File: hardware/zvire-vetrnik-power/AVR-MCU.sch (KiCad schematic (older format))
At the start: 38 parts, among them J10 AC frequency sense, J11 AVR-ISP-6, J12 ACS712_2, J13 ACS712, Q13 BC847, Q14 BC846, SW1 AVR RESET, U1 LTV-847, U8 L78L05_TO92, U9 ATmega8-16PU, Y1 16MHz

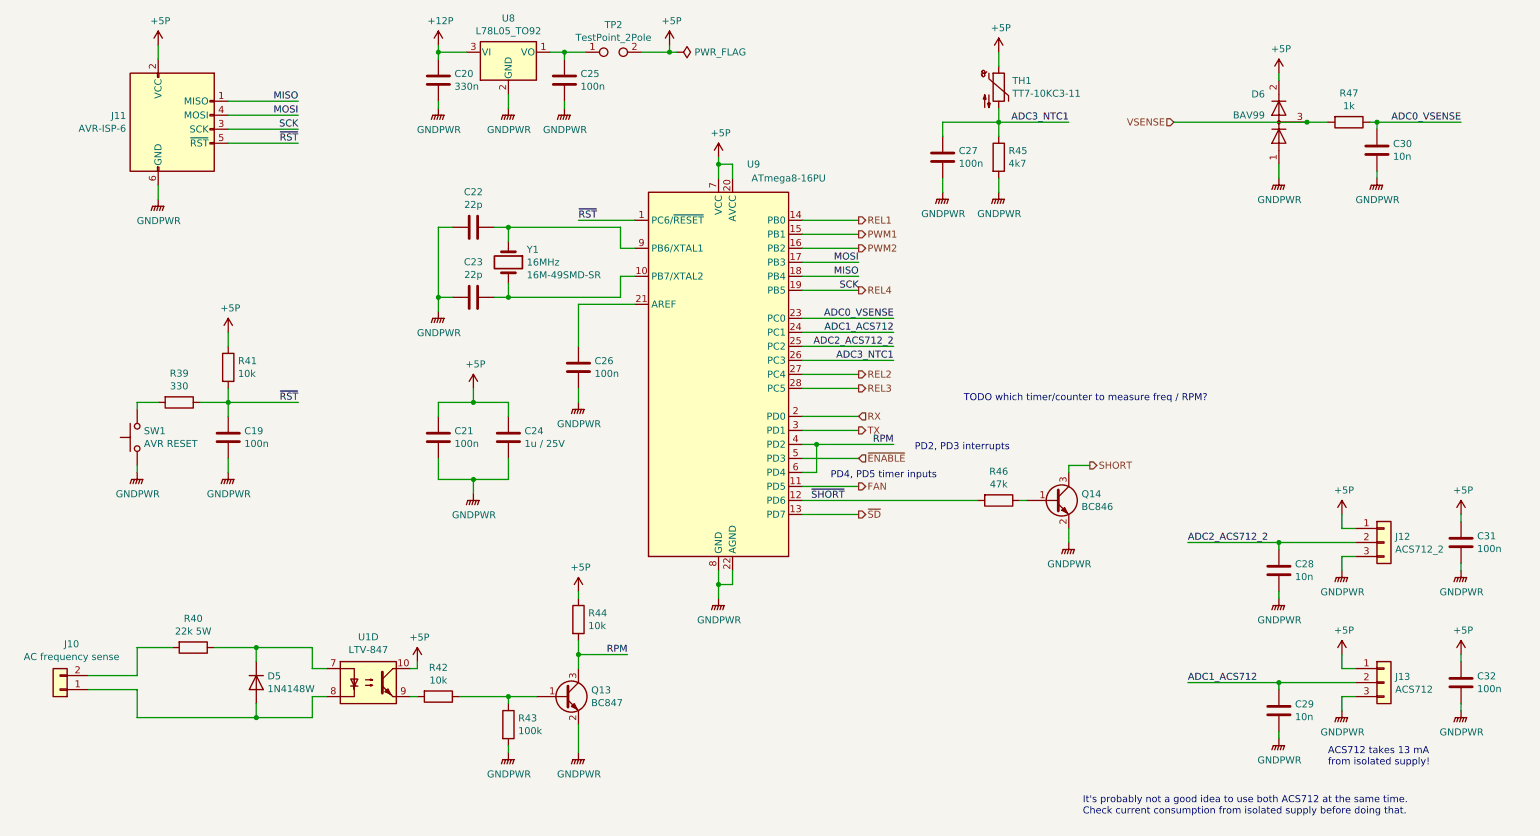
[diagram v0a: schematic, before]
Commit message: Vyrobena verze power PCB
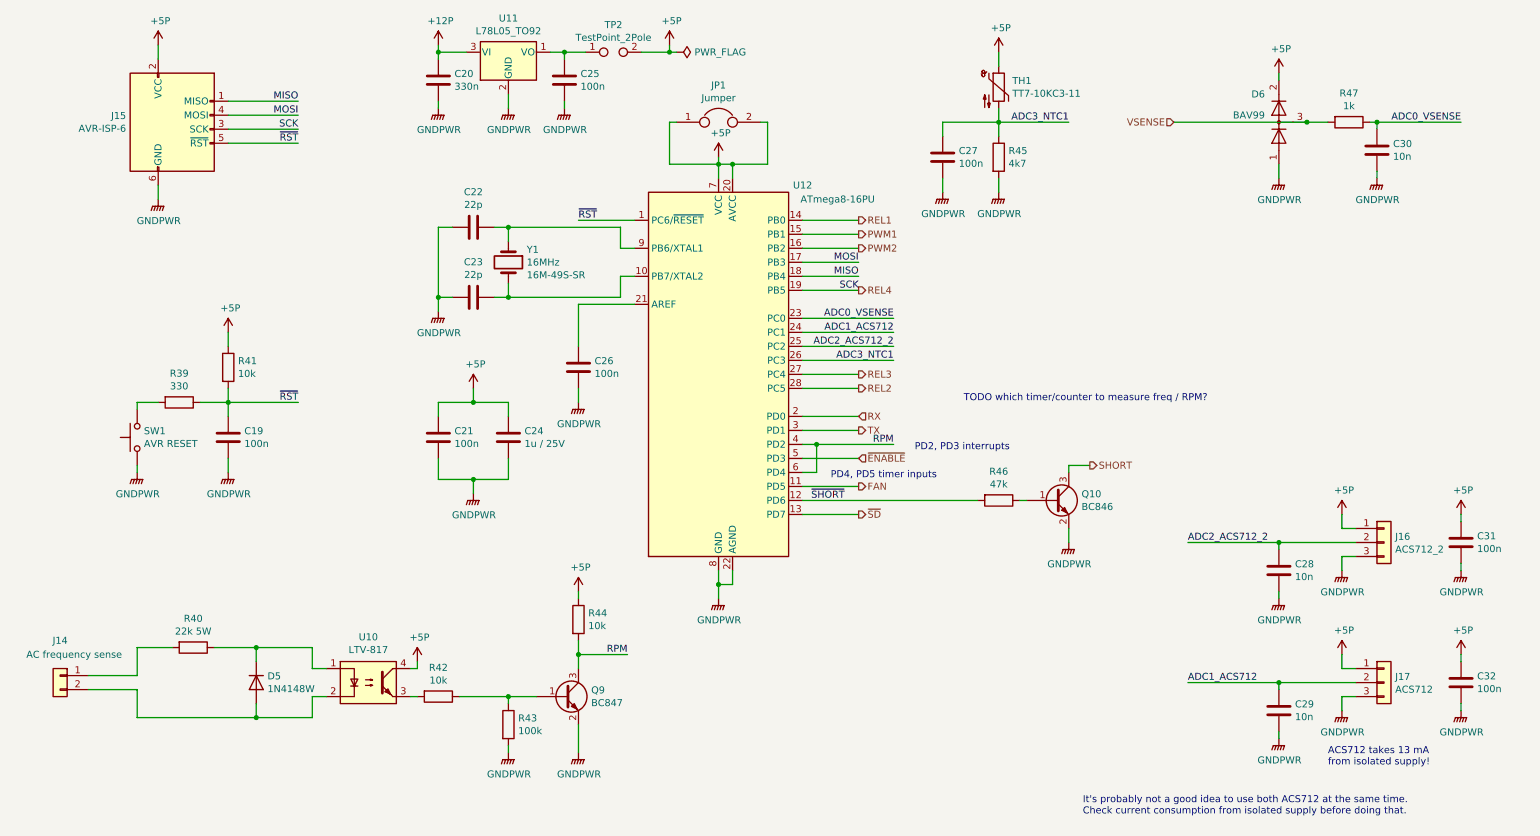
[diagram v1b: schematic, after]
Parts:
- removed U1: LTV-847, Package_DIP:DIP-16_W7.62mm, symbol Isolator:LTV-847
- added JP1: Jumper, Resistor_SMD:R_1206_3216Metric_Pad1.30x1.75mm_HandSolder, symbol Device:Jumper
- added U10: LTV-817, Package_DIP:DIP-4_W7.62mm, symbol Isolator:LTV-817
- TH1: footprint Resistor_THT:R_Axial_DIN0204_L3.6mm_D1.6mm_P2.54mm_Vertical -> Connector_Molex:Molex_KK-254_AE-6410-02A_1x02_P2.54mm_Vertical
- U11: renamed from U8; footprint Package_TO_SOT_THT:TO-92_Inline -> Package_TO_SOT_THT:TO-92L_HandSolder
- U12: renamed from U9; footprint Package_DIP:DIP-28_W7.62mm -> Package_DIP:DIP-28_W7.62mm_Socket
- Y1: footprint Crystal:Crystal_SMD_HC49-SD_HandSoldering -> Crystal:Crystal_HC49-U_Vertical; TME https://www.tme.eu/cz/details/16m-49smd-sr/krystalove-rezon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 -> https://www.tme.eu/cz/details/16m-49s-sr/krystalove-rezonat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; TME Symbol 16M-49SMD-SR -> 16M-49S-SR
- renumbered J10 to J14, J11 to J15, J12 to J16, J13 to J17, Q14 to Q10, Q13 to Q9
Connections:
- net +5P: now also JP1.1, JP1.2, U10.4
- net REL2: now also U12.28 (PC5); no longer U12.27 (PC4)
- net REL3: now also U12.27 (PC4); no longer U12.28 (PC5)
- net at R42.2: now also U10.3
- net at D5.1 (K), R40.1: now also U10.1
- net at D5.2 (A): now also J14.2 (Pin_2), U10.2; no longer J14.1 (Pin_1)
- net at R40.2: now also J14.1 (Pin_1); no longer J14.2 (Pin_2)

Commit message: Add filter cap for noise immunity in RPM circuit
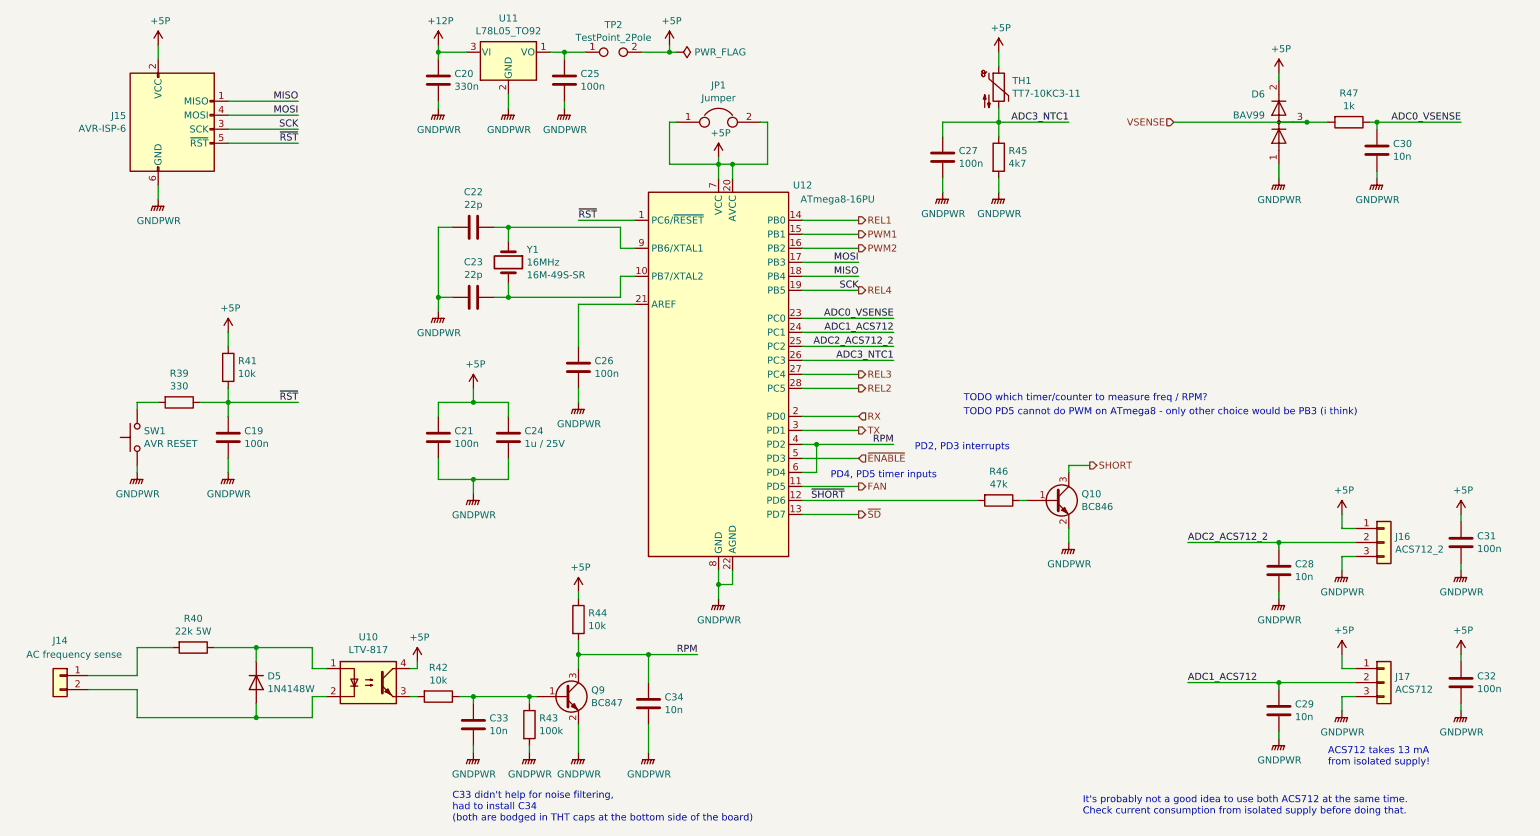
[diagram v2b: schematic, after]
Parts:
- added C33, C34: 10n, Capacitor_SMD:C_1206_3216Metric_Pad1.33x1.80mm_HandSolder, symbol Device:C
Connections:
- net GNDPWR: now also C33.2, C34.2
- net RPM: now also C34.1
- net at Q9.1 (B), R42.1, R43.1: now also C33.1
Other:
- note added: "C33 didn't help for noise filtering,\nhad to install C34\n(both are bodged in THT caps at the bottom side of the board)"
- note added: "TODO PD5 cannot do PWM on ATmega8 - only other choice would be PB3 (i think)"
- moved on the sheet: R43
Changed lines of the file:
@@
 Wire Wire Line
 	4500 5800 4500 6000
-Text Label 4850 5300 2    50   ~ 0
+Text Label 5350 5300 2    50   ~ 0
 RPM
 Text Label 6750 3800 2    50   ~ 0
@@
 	4500 5300 4500 5400
 Wire Wire Line
-	4850 5300 4500 5300
+	5350 5300 5000 5300
 Connection ~ 4500 5300
 $Comp
@@
 L Device:R R43
 U 1 1 63099CF9
-P 4000 5800
-F 0 "R43" H 4070 5846 50  0000 L CNN
-F 1 "100k" H 4070 5755 50  0000 L CNN
-F 2 "Resistor_SMD:R_1206_3216Metric_Pad1.30x1.75mm_HandSolder" V 3930 5800 50  0001 C CNN
-F 3 "~" H 4000 5800 50  0001 C CNN
-	1    4000 5800
-	1    0    0    -1
-$EndComp
-Wire Wire Line
-	3650 5600 4000 5600
-Wire Wire Line
-	4000 5650 4000 5600
-Connection ~ 4000 5600
-Wire Wire Line
-	4000 5600 4200 5600
+P 4150 5800
+F 0 "R43" H 4220 5846 50  0000 L CNN
+F 1 "100k" H 4220 5755 50  0000 L CNN
+F 2 "Resistor_SMD:R_1206_3216Metric_Pad1.30x1.75mm_HandSolder" V 4080 5800 50  0001 C CNN
+F 3 "~" H 4150 5800 50  0001 C CNN
+	1    4150 5800
+	1    0    0    -1
+$EndComp
+Wire Wire Line
+	3650 5600 3750 5600
+Wire Wire Line
+	4150 5650 4150 5600
+Connection ~ 4150 5600
+Wire Wire Line
+	4150 5600 4200 5600
 $Comp
 L power:GNDPWR #PWR085
 U 1 1 630AFFFF
-P 4000 6000
-F 0 "#PWR085" H 4000 5800 50  0001 C CNN
-F 1 "GNDPWR" H 4004 5846 50  0000 C CNN
-F 2 "" H 4000 5950 50  0001 C CNN
-F 3 "" H 4000 5950 50  0001 C CNN
-	1    4000 6000
-	1    0    0    -1
-$EndComp
-Wire Wire Line
-	4000 6000 4000 5950
+P 4150 6000
+F 0 "#PWR085" H 4150 5800 50  0001 C CNN
+F 1 "GNDPWR" H 4154 5846 50  0000 C CNN
+F 2 "" H 4150 5950 50  0001 C CNN
+F 3 "" H 4150 5950 50  0001 C CNN
+	1    4150 6000
+	1    0    0    -1
+$EndComp
+Wire Wire Line
+	4150 6000 4150 5950
 Wire Wire Line
 	1350 5750 2200 5750
@@
 Text Label 6750 3100 2    50   ~ 0
 ADC2_ACS712_2
+Text Notes 3600 6500 0    50   ~ 0
+C33 didn't help for noise filtering,\nhad to install C34\n(both are bodged in THT caps at the bottom side of the board)
+Text Notes 7250 3600 0    50   ~ 0
+TODO PD5 cannot do PWM on ATmega8 - only other choice would be PB3 (i think)
+$Comp
+L Device:C C33
+U 1 1 63304B82
+P 3750 5800
+F 0 "C33" H 3865 5846 50  0000 L CNN
+F 1 "10n" H 3865 5755 50  0000 L CNN
+F 2 "Capacitor_SMD:C_1206_3216Metric_Pad1.33x1.80mm_HandSolder" H 3788 5650 50  0001 C CNN
+F 3 "~" H 3750 5800 50  0001 C CNN
+	1    3750 5800
+	1    0    0    -1
+$EndComp
+Wire Wire Line
+	3750 5650 3750 5600
+Connection ~ 3750 5600
+Wire Wire Line
+	3750 5600 4150 5600
+$Comp
+L power:GNDPWR #PWR014
+U 1 1 6332AD1C
+P 3750 6000
+F 0 "#PWR014" H 3750 5800 50  0001 C CNN
+F 1 "GNDPWR" H 3754 5846 50  0000 C CNN
+F 2 "" H 3750 5950 50  0001 C CNN
+F 3 "" H 3750 5950 50  0001 C CNN
+	1    3750 6000
+	1    0    0    -1
+$EndComp
+Wire Wire Line
+	3750 6000 3750 5950
+$Comp
+L Device:C C34
+U 1 1 63334906
+P 5000 5650
+F 0 "C34" H 5115 5696 50  0000 L CNN
+F 1 "10n" H 5115 5605 50  0000 L CNN
+F 2 "Capacitor_SMD:C_1206_3216Metric_Pad1.33x1.80mm_HandSolder" H 5038 5500 50  0001 C CNN
+F 3 "~" H 5000 5650 50  0001 C CNN
+	1    5000 5650
+	1    0    0    -1
+$EndComp
+$Comp
+L power:GNDPWR #PWR021
+U 1 1 63334EB6
+P 5000 6000
+F 0 "#PWR021" H 5000 5800 50  0001 C CNN
+F 1 "GNDPWR" H 5004 5846 50  0000 C CNN
+F 2 "" H 5000 5950 50  0001 C CNN
+F 3 "" H 5000 5950 50  0001 C CNN
+	1    5000 6000
+	1    0    0    -1
+$EndComp
+Wire Wire Line
+	5000 6000 5000 5800
+Wire Wire Line
+	5000 5500 5000 5300
+Connection ~ 5000 5300
+Wire Wire Line
+	5000 5300 4500 5300
 $EndSCHEMATC

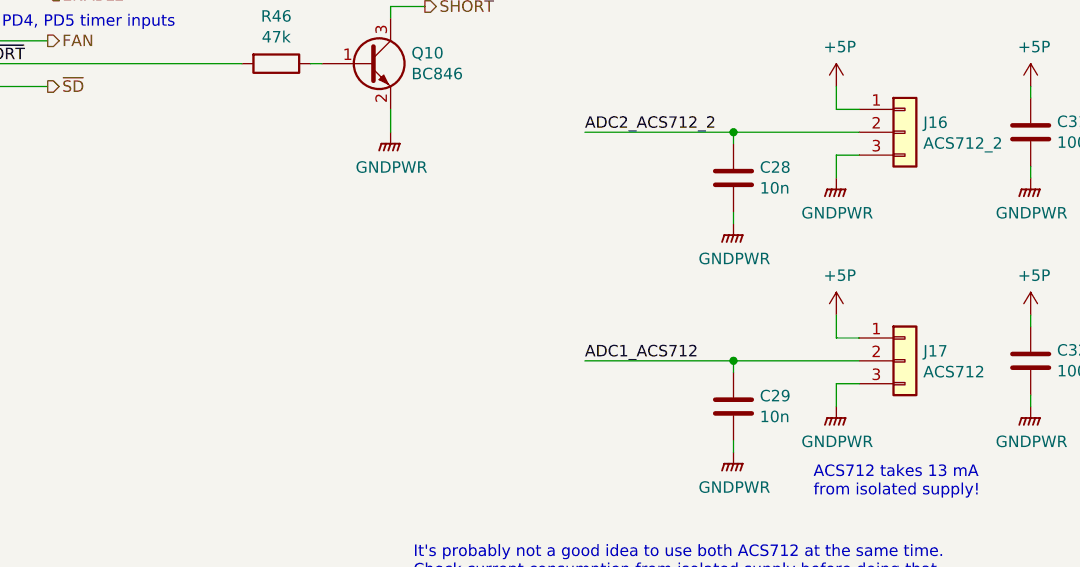
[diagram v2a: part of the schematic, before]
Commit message: [power] Add extra NTC for rectifier heatsink
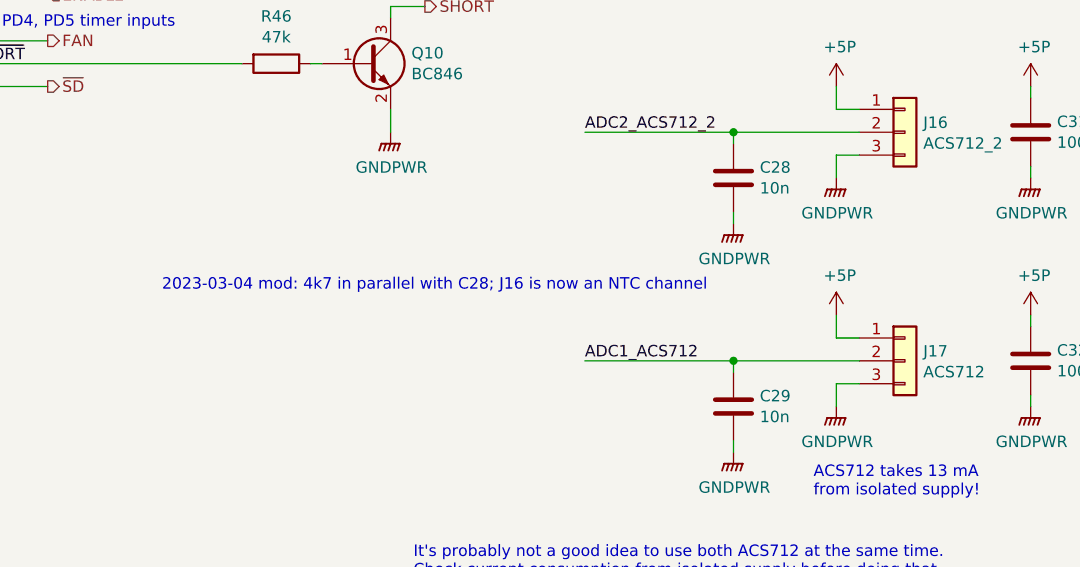
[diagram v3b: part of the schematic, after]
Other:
- note added: "2023-03-04 mod: 4k7 in parallel with C28; J16 is now an NTC channel"
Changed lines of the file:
@@
 Wire Wire Line
 	5000 5300 4500 5300
+Text Notes 7000 5200 0    50   ~ 0
+2023-03-04 mod: 4k7 in parallel with C28; J16 is now an NTC channel
 $EndSCHEMATC
